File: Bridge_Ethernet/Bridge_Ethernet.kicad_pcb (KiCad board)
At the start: 2 copper layers, 82 parts, among them J1 Conn_01x04_Female, J2 Conn_01x04_Female, J3 Conn_01x06, J4 Conn_01x06, J5 Conn_2Rows-13Pins, J7 Conn_01x04_Male, U1 MAX3222CDW, U10 MAX3222CDW, U11 ISL83485, U12 MAX3222CDW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

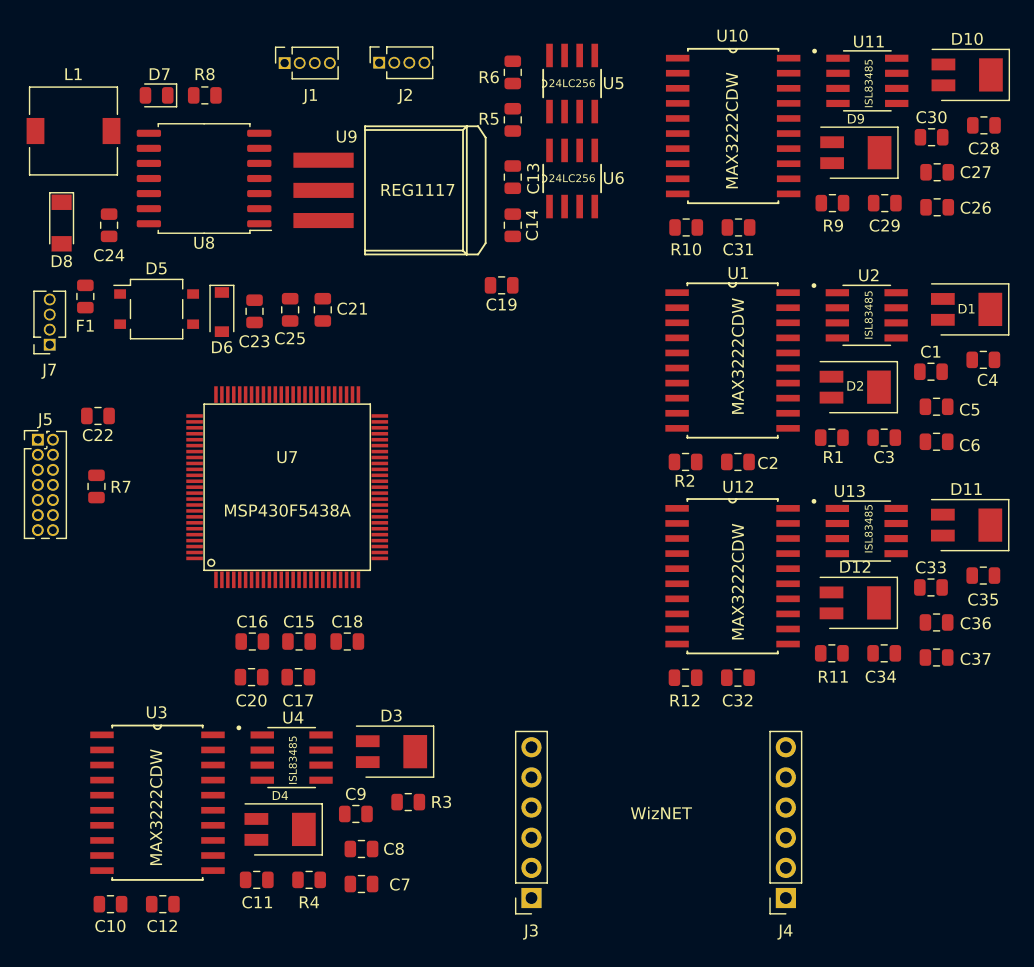
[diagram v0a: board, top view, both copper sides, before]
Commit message: Esquemático Finalizado. Asignaciones Realizadas. Componentes acomodados en PCB v2.0.
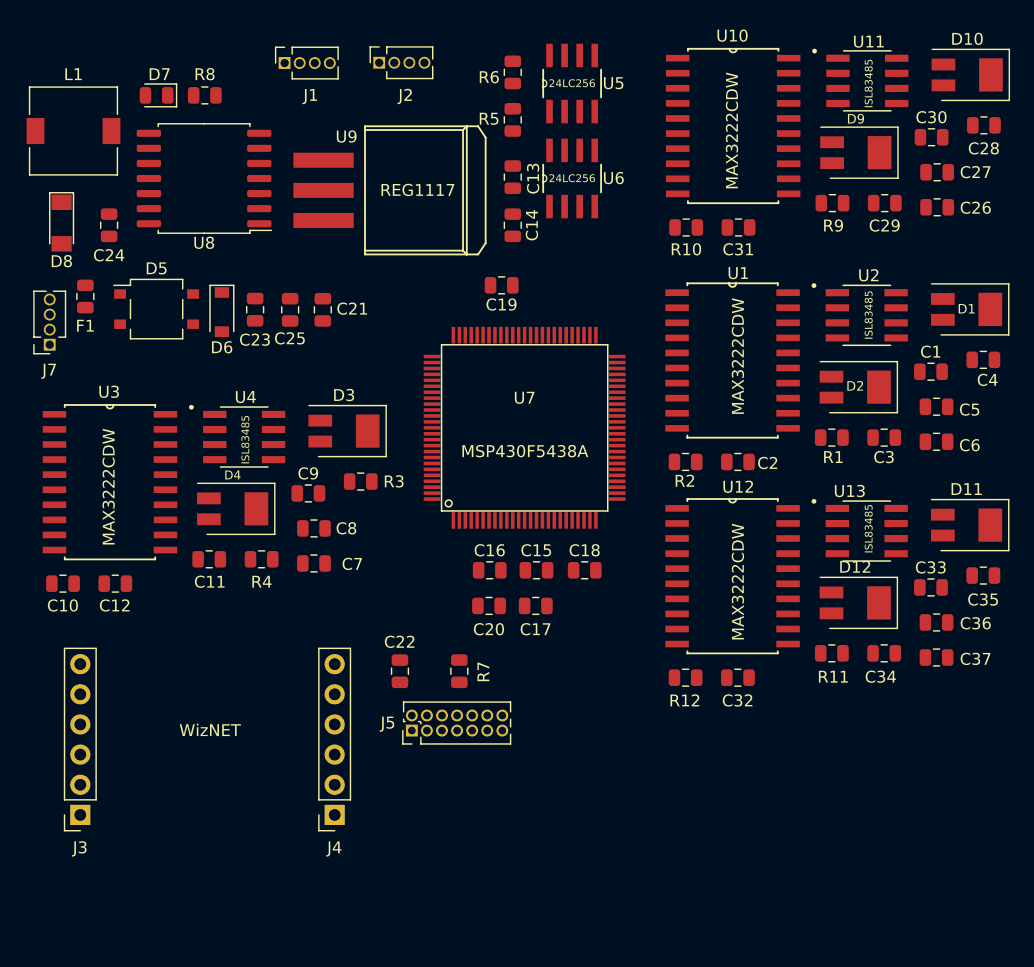
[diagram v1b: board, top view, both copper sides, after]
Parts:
- moved J5 39.9 mm to (61.5, 111.5), turned to 90 degrees
- moved J3 38.6 mm to (33.6, 118.6)
- moved J4 38.6 mm to (55.0, 118.6)
- moved R7 34.3 mm to (65.5, 106.5)
- moved C22 33.3 mm to (60.5, 106.5), turned to 270 degrees
- moved C10 27.3 mm to (32.1, 99.1)
- moved C11 27.3 mm to (44.4, 97.1)
- moved C12 27.3 mm to (36.5, 99.1)
- moved C7 27.3 mm to (53.3, 97.4)
- moved C8 27.3 mm to (53.3, 94.5)
- moved C9 27.3 mm to (52.8, 91.5)
- moved D3 27.3 mm to (55.8, 86.3)
- moved D4 27.3 mm to (46.4, 92.8)
- moved R3 27.3 mm to (57.2, 90.5)
- moved R4 27.3 mm to (48.8, 97.1)
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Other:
- board text added: "Alimentación"
- board text added: "Drivers Serie 0, 1 y 2"
- board text added: "Drivers Serie 3"
- board text added: "Memorias"
- board text added: "Micro"
